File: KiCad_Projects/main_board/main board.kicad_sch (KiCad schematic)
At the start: 21 parts

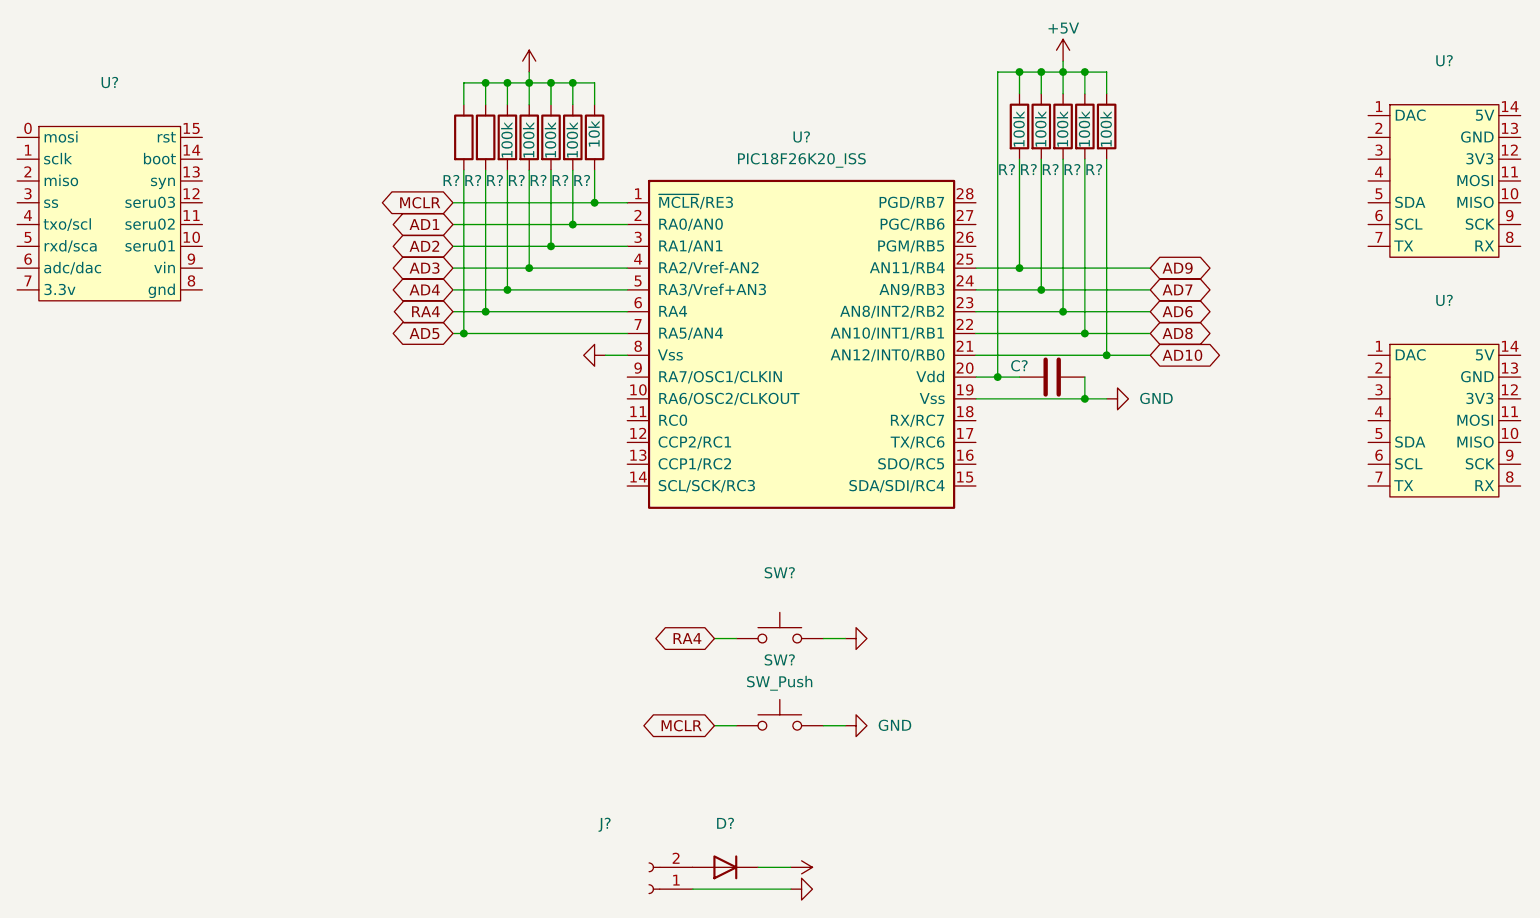
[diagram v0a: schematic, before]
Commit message: シンボルライブラリのパス指定を絶対パスから相対パスへ変更。
環境によってプロジェクトの配置階層が変わるのでプロジェクトから見た相対パスへ変更。
${KIPRJMOD}/../Lib/(project_name)
で指定可能なのでこれからはそうすること。
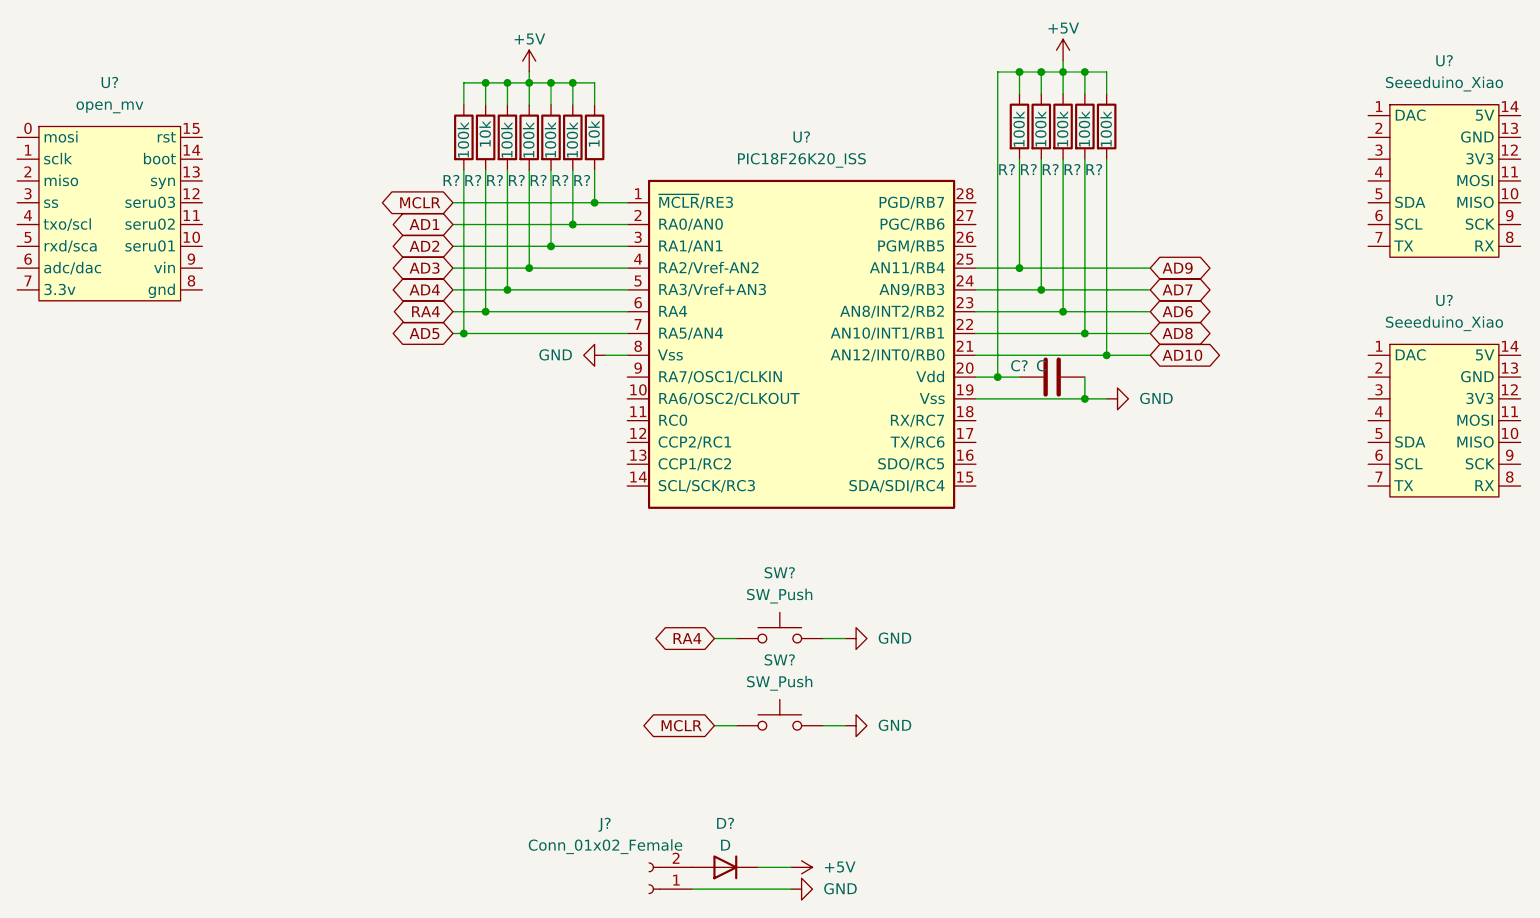
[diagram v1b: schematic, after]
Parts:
- C?: value (none) -> C
- D?: value (none) -> D
- J?: value (none) -> Conn_01x02_Female
- R?: value (none) -> 100k
- R?: value (none) -> 10k
- SW?: value (none) -> SW_Push
- U? (x2): value (none) -> Seeeduino_Xiao
- U?: value (none) -> open_mv
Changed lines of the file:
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@@
       (effects (font (size 1.27 1.27)) hide)
     )
-    (property "Value" "" (id 1) (at 121.92 97.7899 90)
+    (property "Value" "GND" (id 1) (at 121.92 97.7899 90)
       (effects (font (size 1.27 1.27)) (justify right))
     )
@@
       (effects (font (size 1.27 1.27)) hide)
     )
-    (property "Value" "" (id 1) (at 116.84 60.96 0))
+    (property "Value" "+5V" (id 1) (at 116.84 60.96 0))
     (property "Footprint" "" (id 2) (at 116.84 64.77 0)
       (effects (font (size 1.27 1.27)) hide)
@@
     (in_bom yes) (on_board yes)
     (property "Reference" "D?" (id 0) (at 139.7 152.4 0))
-    (property "Value" "" (id 1) (at 139.7 154.94 0))
+    (property "Value" "D" (id 1) (at 139.7 154.94 0))
     (property "Footprint" "" (id 2) (at 139.7 157.48 0)
       (effects (font (size 1.27 1.27)) hide)
@@
       (effects (font (size 1.27 1.27)) (justify left))
     )
-    (property "Value" "" (id 1) (at 109.22 74.93 90)
+    (property "Value" "100k" (id 1) (at 109.22 74.93 90)
       (effects (font (size 1.27 1.27)) (justify left))
     )
@@
       (effects (font (size 1.27 1.27)) (justify left))
     )
-    (property "Value" "" (id 1) (at 111.76 73.66 90)
+    (property "Value" "10k" (id 1) (at 111.76 73.66 90)
       (effects (font (size 1.27 1.27)) (justify left))
     )
@@
     (in_bom yes) (on_board yes)
     (property "Reference" "U?" (id 0) (at 223.52 91.44 0))
-    (property "Value" "" (id 1) (at 223.52 93.98 0))
+    (property "Value" "Seeeduino_Xiao" (id 1) (at 223.52 93.98 0))
     (property "Footprint" "" (id 2) (at 222.25 99.06 0)
       (effects (font (size 1.27 1.27)) hide)
@@
     (in_bom yes) (on_board yes) (fields_autoplaced)
     (property "Reference" "U?" (id 0) (at 223.52 63.5 0))
-    (property "Value" "" (id 1) (at 223.52 66.04 0))
+    (property "Value" "Seeeduino_Xiao" (id 1) (at 223.52 66.04 0))
     (property "Footprint" "" (id 2) (at 222.25 71.12 0)
       (effects (font (size 1.27 1.27)) hide)
@@
       (effects (font (size 1.27 1.27)) hide)
     )
-    (property "Value" "" (id 1) (at 151.13 160.0199 90)
+    (property "Value" "GND" (id 1) (at 151.13 160.0199 90)
       (effects (font (size 1.27 1.27)) (justify right))
     )
@@
     (in_bom yes) (on_board yes)
     (property "Reference" "J?" (id 0) (at 125.73 152.4 0))
-    (property "Value" "" (id 1) (at 125.73 154.94 0))
+    (property "Value" "Conn_01x02_Female" (id 1) (at 125.73 154.94 0))
     (property "Footprint" "" (id 2) (at 130.81 160.02 0)
       (effects (font (size 1.27 1.27)) hide)
@@
     (in_bom yes) (on_board yes)
     (property "Reference" "C?" (id 0) (at 173.99 99.06 90))
-    (property "Value" "" (id 1) (at 176.53 99.06 90))
+    (property "Value" "C" (id 1) (at 176.53 99.06 90))
     (property "Footprint" "" (id 2) (at 181.61 99.3648 0)
       (effects (font (size 1.27 1.27)) hide)
@@
       (effects (font (size 1.27 1.27)) hide)
     )
-    (property "Value" "" (id 1) (at 151.13 157.4799 90)
+    (property "Value" "+5V" (id 1) (at 151.13 157.4799 90)
       (effects (font (size 1.27 1.27)) (justify left))
     )
@@
     (in_bom yes) (on_board yes) (fields_autoplaced)
     (property "Reference" "U?" (id 0) (at 67.945 66.04 0))
-    (property "Value" "" (id 1) (at 67.945 68.58 0))
+    (property "Value" "open_mv" (id 1) (at 67.945 68.58 0))
     (property "Footprint" "" (id 2) (at 67.31 71.12 0)
       (effects (font (size 1.27 1.27)) hide)
@@
       (effects (font (size 1.27 1.27)) hide)
     )
-    (property "Value" "" (id 1) (at 157.48 130.8099 90)
+    (property "Value" "GND" (id 1) (at 157.48 130.8099 90)
       (effects (font (size 1.27 1.27)) (justify right))
     )
@@
     (in_bom yes) (on_board yes) (fields_autoplaced)
     (property "Reference" "SW?" (id 0) (at 146.05 123.19 0))
-    (property "Value" "" (id 1) (at 146.05 125.73 0))
+    (property "Value" "SW_Push" (id 1) (at 146.05 125.73 0))
     (property "Footprint" "" (id 2) (at 146.05 125.73 0)
       (effects (font (size 1.27 1.27)) hide)

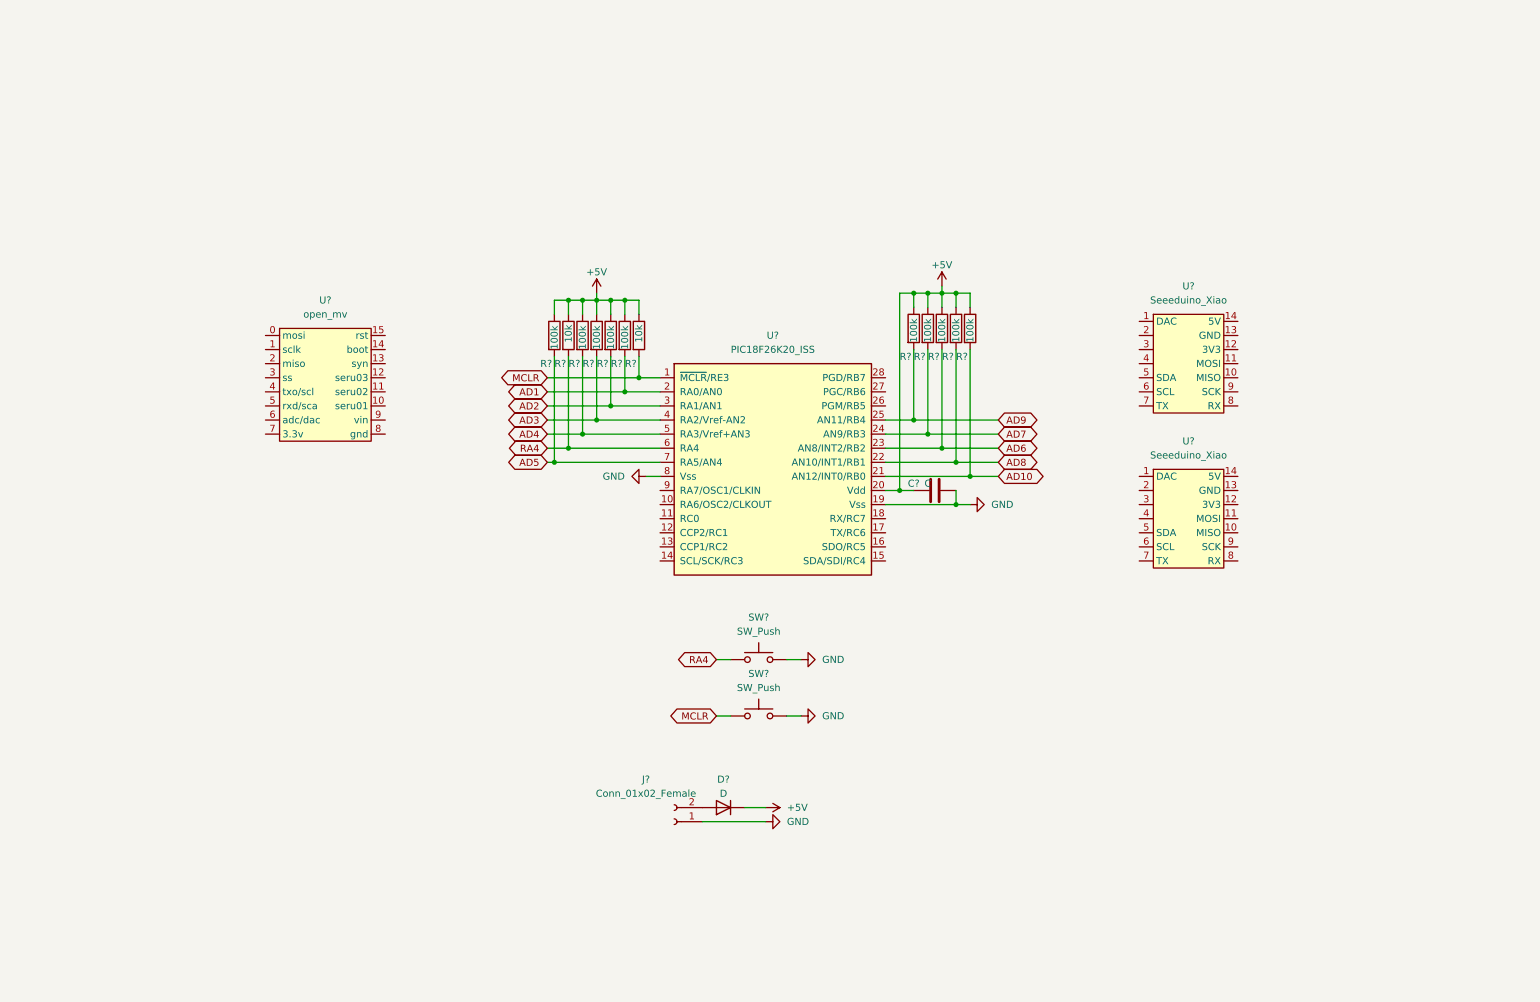
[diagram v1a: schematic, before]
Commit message: メイン基板の更新
IRセンサー等のセンサー追加、配線追加。
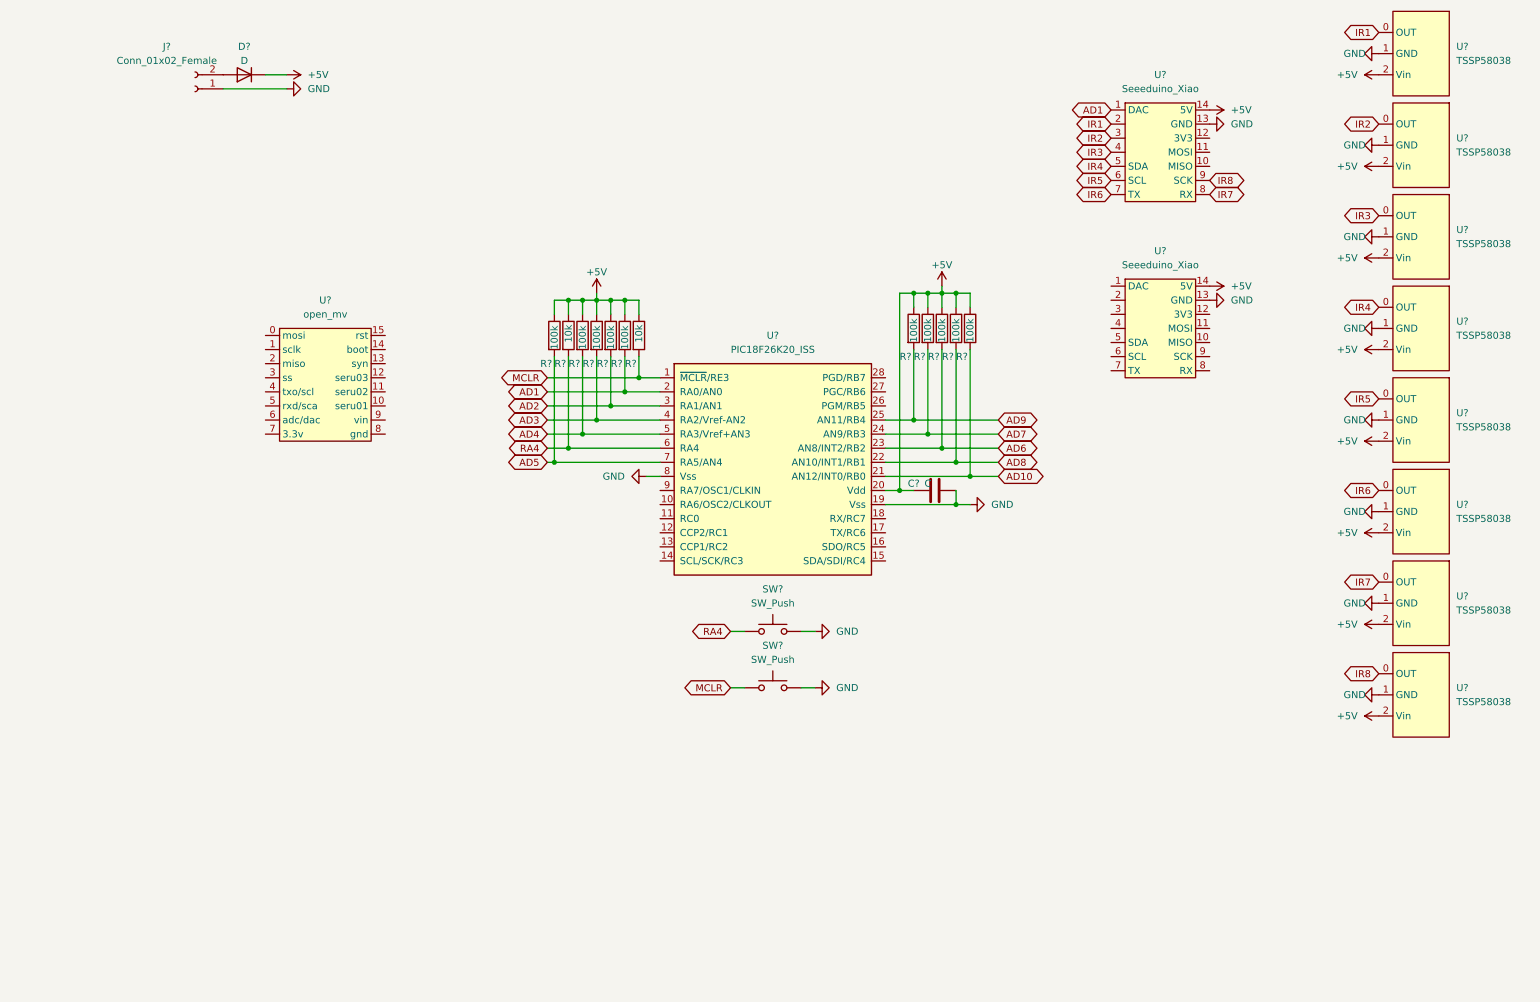
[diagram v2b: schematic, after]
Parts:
- added U? (x8): TSSP58038, symbol ir_sensor:TSSP58038
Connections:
- net +5V: now also U?.14 (5V), U?.14 (5V), U?.2 (Vin), U?.2 (Vin), U?.2 (Vin), U?.2 (Vin), U?.2 (Vin), U?.2 (Vin), U?.2 (Vin), U?.2 (Vin)
- net AD1: now also U?.1 (DAC)
- net GND: now also U?.13 (GND), U?.13 (GND), U?.1 (GND), U?.1 (GND), U?.1 (GND), U?.1 (GND), U?.1 (GND), U?.1 (GND), U?.1 (GND), U?.1 (GND)
- net IR1: now reaches U?.2
- net IR1: now also U?.0 (OUT)
- net IR2: now reaches U?.3
- net IR2: now also U?.0 (OUT)
- net IR3: now reaches U?.4
- net IR3: now also U?.0 (OUT)
- net IR4: now reaches U?.5 (SDA)
- net IR4: now also U?.0 (OUT)
- net IR5: now reaches U?.6 (SCL)
- net IR5: now also U?.0 (OUT)
- net IR6: now reaches U?.7 (TX)
- net IR6: now also U?.0 (OUT)
- net IR7: now reaches U?.8 (RX)
- net IR7: now also U?.0 (OUT)
- net IR8: now reaches U?.9 (SCK)
- net IR8: now also U?.0 (OUT)
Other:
- moved on the sheet: D?, J?, SW?, U?

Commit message: メイン基板の更新
IRセンサの配線変更等
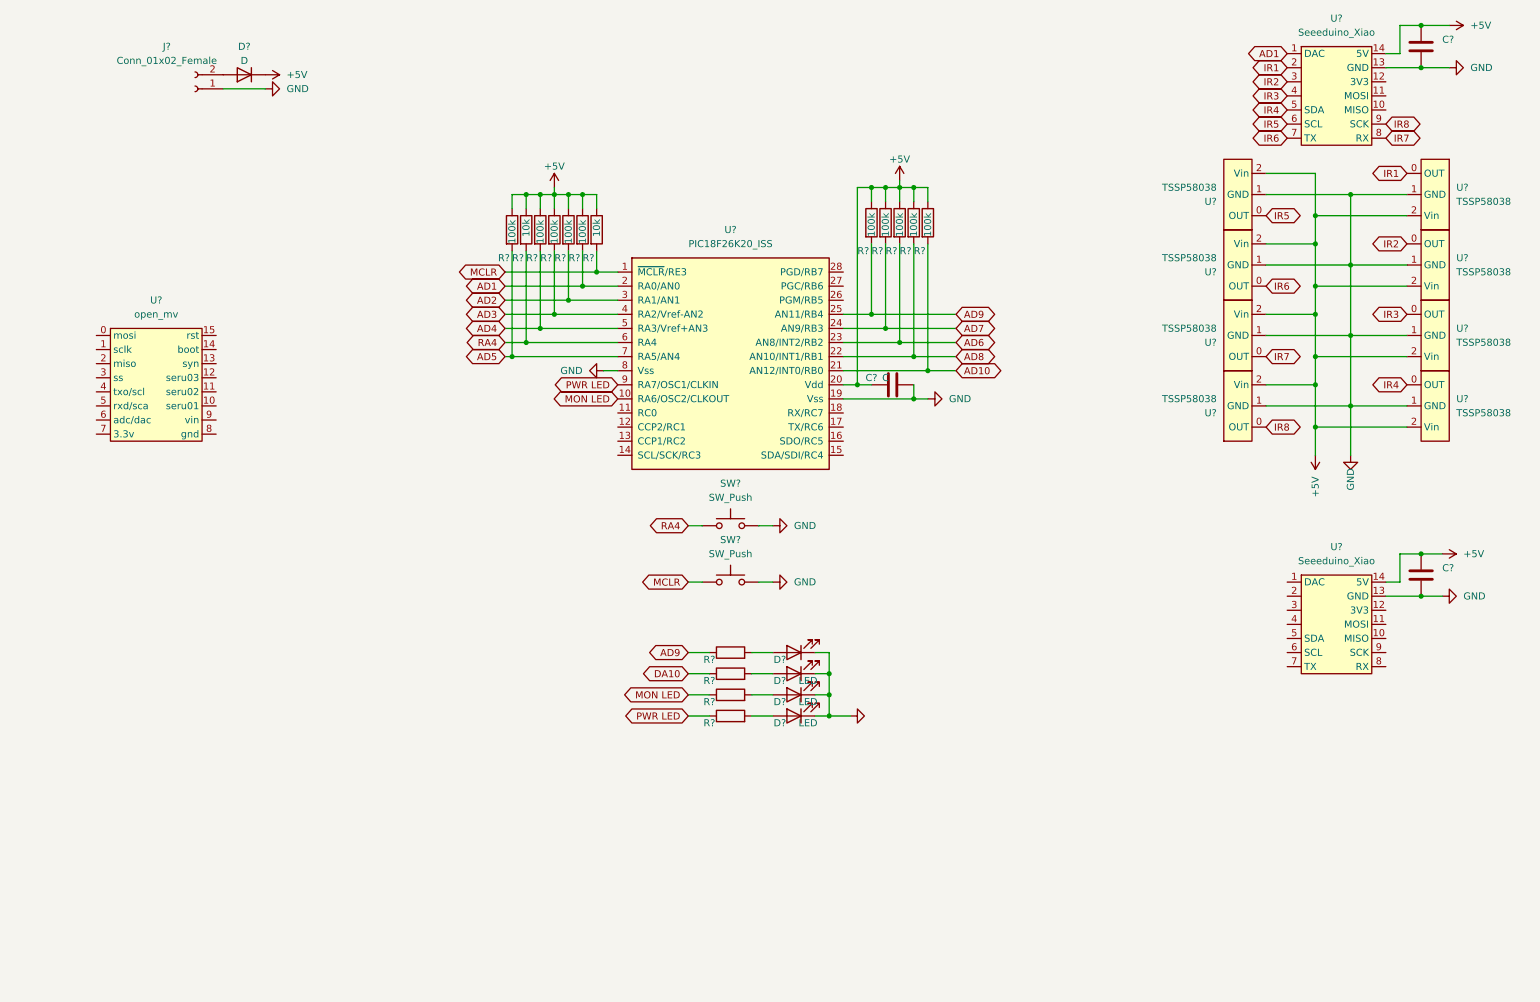
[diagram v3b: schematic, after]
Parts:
- removed U? (x3): TSSP58038, symbol ir_sensor:TSSP58038
- added C? (x2): (no value), symbol Device:C
- added D? (x3): LED, symbol Device:LED
- added D?: (no value), symbol Device:LED
- added R? (x4): (no value), symbol Device:R
- added U? (x3): TSSP58038, symbol ir_sensor:TSSP58038
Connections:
- net +5V: now also C?.1, C?.1, U?.2 (Vin), U?.2 (Vin), U?.2 (Vin)
- net AD9: now also R?.1
- net GND: now also C?.2, C?.2, D?.1 (K), D?.1 (K), D?.1 (K), D?.1 (K), U?.1 (GND), U?.1 (GND), U?.1 (GND)
- net IR5: now also U?.0 (OUT)
- net IR6: now also U?.0 (OUT)
- net IR7: now also U?.0 (OUT)
- net IR8: now also U?.0 (OUT); no longer U?.0 (OUT)
- net MON LED: now reaches U?.10 (RA6/OSC2/CLKOUT)
- net MON LED: now also R?.1
- net PWR LED: now reaches U?.9 (RA7/OSC1/CLKIN)
- net PWR LED: now also R?.1
- new net: D?.2 (A), R?.2 (x4)
- new net DA10: R?.1
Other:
- moved on the sheet: C?, R?, SW?, U?

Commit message: メイン基板の更新
内容は知らないです
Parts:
- added C? (x7): C_Small, symbol Device:C_Small
- added C?: (no value), symbol Device:C_Small
- added J?: Conn_01x04_Female, symbol Connector:Conn_01x04_Female
- added J?: (no value), symbol Connector:Conn_01x04_Female
- added R? (x7): R, symbol Device:R
- added R? (x5): (no value), symbol Device:R
- added R?: (no value), symbol Device:R_Variable
- added U?: (no value), symbol mpu6050:MPU6050
- C? (x2): value (none) -> C
- D?: value (none) -> LED
- R? (x4): value (none) -> 330
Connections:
- net +5V: now also C?.1, C?.1, C?.1, C?.1, J?.3 (Pin_3), J?.4 (Pin_4), R?.1, R?.1, R?.1, R?.2, R?.2, R?.2, R?.2; no longer U?.2 (Vin), U?.2 (Vin), U?.2 (Vin), U?.2 (Vin), U?.2 (Vin), U?.2 (Vin), U?.2 (Vin), U?.2 (Vin)
- net AD6: now also J?.2 (Pin_2)
- net GND: now also C?.1, C?.1, C?.1, C?.1, C?.2, C?.2, C?.2, C?.2, C?.2, C?.2, C?.2, C?.2, J?.1 (Pin_1), J?.3 (Pin_3), R?.1, R?.1, R?.1, R?.1
- net SCL: now reaches U?.14 (SCL/SCK/RC3)
- net SCL: now also R?.2, R?.2
- net SDA: now reaches U?.15 (SDA/SDI/RC4)
- net SDA: now also R?.2, R?.2
- new net: R?.2, U?.2 (Vin) (x4)
- new net: R?.1, U?.2 (Vin) (x4)
- new net: J?.2 (Pin_2), R?.1
- new net: J?.1 (Pin_1), R?.2
- new net: J?.4 (Pin_4), R?.1
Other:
- moved on the sheet: C?, U?
